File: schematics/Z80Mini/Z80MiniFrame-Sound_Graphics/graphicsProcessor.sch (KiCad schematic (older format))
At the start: 18 parts, among them J2 RGB Out, U1 TMS9929A, U12 74LS32, U2 74LS574, U3 74LS574, U4 74LS574, U5 AS6C62256-55PCN, U6 74HC04, Y1 Crystal

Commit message: Latest graphics and sound card schematic and PCB modifications
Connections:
- wire segments 226 -> 227
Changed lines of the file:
@@
 L power:VCC #PWR0103
 U 1 1 5D7AF4D2
-P 9100 750
-F 0 "#PWR0103" H 9100 600 50  0001 C CNN
-F 1 "VCC" H 9117 923 50  0000 C CNN
-F 2 "" H 9100 750 50  0001 C CNN
-F 3 "" H 9100 750 50  0001 C CNN
-	1    9100 750
+P 7850 750
+F 0 "#PWR0103" H 7850 600 50  0001 C CNN
+F 1 "VCC" H 7867 923 50  0000 C CNN
+F 2 "" H 7850 750 50  0001 C CNN
+F 3 "" H 7850 750 50  0001 C CNN
+	1    7850 750
 	1    0    0    -1
 $EndComp
@@
 	6600 950  6600 850
 Wire Wire Line
-	6600 850  9100 850
+	6600 850  7850 850
 Connection ~ 9100 850
 Wire Wire Line
-	9100 850  9100 750
+	7850 850  7850 750
 Wire Wire Line
 	7100 1350 7250 1350
@@
 Wire Wire Line
 	1250 2500 1650 2500
-Wire Wire Line
-	3950 2350 4250 2350
-Wire Wire Line
-	9000 1450 9800 1450
-Wire Wire Line
-	9000 1950 9700 1950
-Wire Bus Line
-	7700 2450 7700 3000
-Wire Bus Line
-	9250 2350 9250 3000
-Wire Bus Line
-	9250 1050 9250 1950
-Wire Bus Line
-	2800 1050 2800 2950
-Wire Bus Line
-	4150 3350 4150 6850
-Wire Bus Line
-	4150 1050 4150 3050
-Wire Bus Line
-	7800 1050 7800 2150
-Wire Bus Line
-	7350 1050 7350 3700
-Wire Bus Line
-	7700 3000 7700 6850
-Wire Bus Line
-	5850 1050 5850 5550
 $Comp
 L power:GND #PWR0145
@@
 $EndComp
 Connection ~ 1650 1500
+Connection ~ 7850 850
+Wire Wire Line
+	7850 850  9100 850
+Wire Wire Line
+	3950 2350 4250 2350
+Wire Wire Line
+	9000 1450 9800 1450
+Wire Wire Line
+	9000 1950 9700 1950
+Wire Bus Line
+	7700 2450 7700 3000
+Wire Bus Line
+	9250 2350 9250 3000
+Wire Bus Line
+	9250 1050 9250 1950
+Wire Bus Line
+	2800 1050 2800 2950
+Wire Bus Line
+	4150 3350 4150 6850
+Wire Bus Line
+	4150 1050 4150 3050
+Wire Bus Line
+	7800 1050 7800 2150
+Wire Bus Line
+	7350 1050 7350 3700
+Wire Bus Line
+	7700 3000 7700 6850
+Wire Bus Line
+	5850 1050 5850 5550
 $EndSCHEMATC

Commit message: Latest modifications
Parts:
- C16, C17: value 100nF -> 22pF
- U1: symbol Video:TMS9929A -> Z80MiniFrame-Sound_Graphics-rescue:TMS9929A-Video
- U5: symbol Memory_RAM:AS6C62256-55PCN -> Z80MiniFrame-Sound_Graphics-rescue:AS6C62256-55PCN-Memory_RAM
- Y1: value Crystal -> 10MHz
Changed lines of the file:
@@
 $EndDescr
 $Comp
-L Video:TMS9929A U1
+L Z80MiniFrame-Sound_Graphics-rescue:TMS9929A-Video U1
 U 1 1 5D79CD27
 P 3400 1950
@@
 	7350 1050 7800 1050
 $Comp
-L Memory_RAM:AS6C62256-55PCN U5
+L Z80MiniFrame-Sound_Graphics-rescue:AS6C62256-55PCN-Memory_RAM U5
 U 1 1 5D7A4B8E
 P 8000 1350
@@
 P 2000 3150
 F 0 "Y1" V 1954 3281 50  0000 L CNN
-F 1 "Crystal" V 2045 3281 50  0000 L CNN
+F 1 "10MHz" V 2045 3281 50  0000 L CNN
 F 2 "Crystal:Crystal_HC18-U_Vertical" H 2000 3150 50  0001 C CNN
 F 3 "~" H 2000 3150 50  0001 C CNN
@@
 AR Path="/5D79B46A/5DF21B0E" Ref="C16"  Part="1"
 F 0 "C16" V 1348 3000 50  0000 C CNN
-F 1 "100nF" V 1439 3000 50  0000 C CNN
+F 1 "22pF" V 1439 3000 50  0000 C CNN
 F 2 "Capacitor_THT:C_Disc_D7.0mm_W2.5mm_P5.00mm" H 1638 2850 50  0001 C CNN
 F 3 "~" H 1600 3000 50  0001 C CNN
@@
 AR Path="/5D79B46A/5DF22922" Ref="C17"  Part="1"
 F 0 "C17" V 1348 3300 50  0000 C CNN
-F 1 "100nF" V 1439 3300 50  0000 C CNN
+F 1 "22pF" V 1439 3300 50  0000 C CNN
 F 2 "Capacitor_THT:C_Disc_D7.0mm_W2.5mm_P5.00mm" H 1638 3150 50  0001 C CNN
 F 3 "~" H 1600 3300 50  0001 C CNN

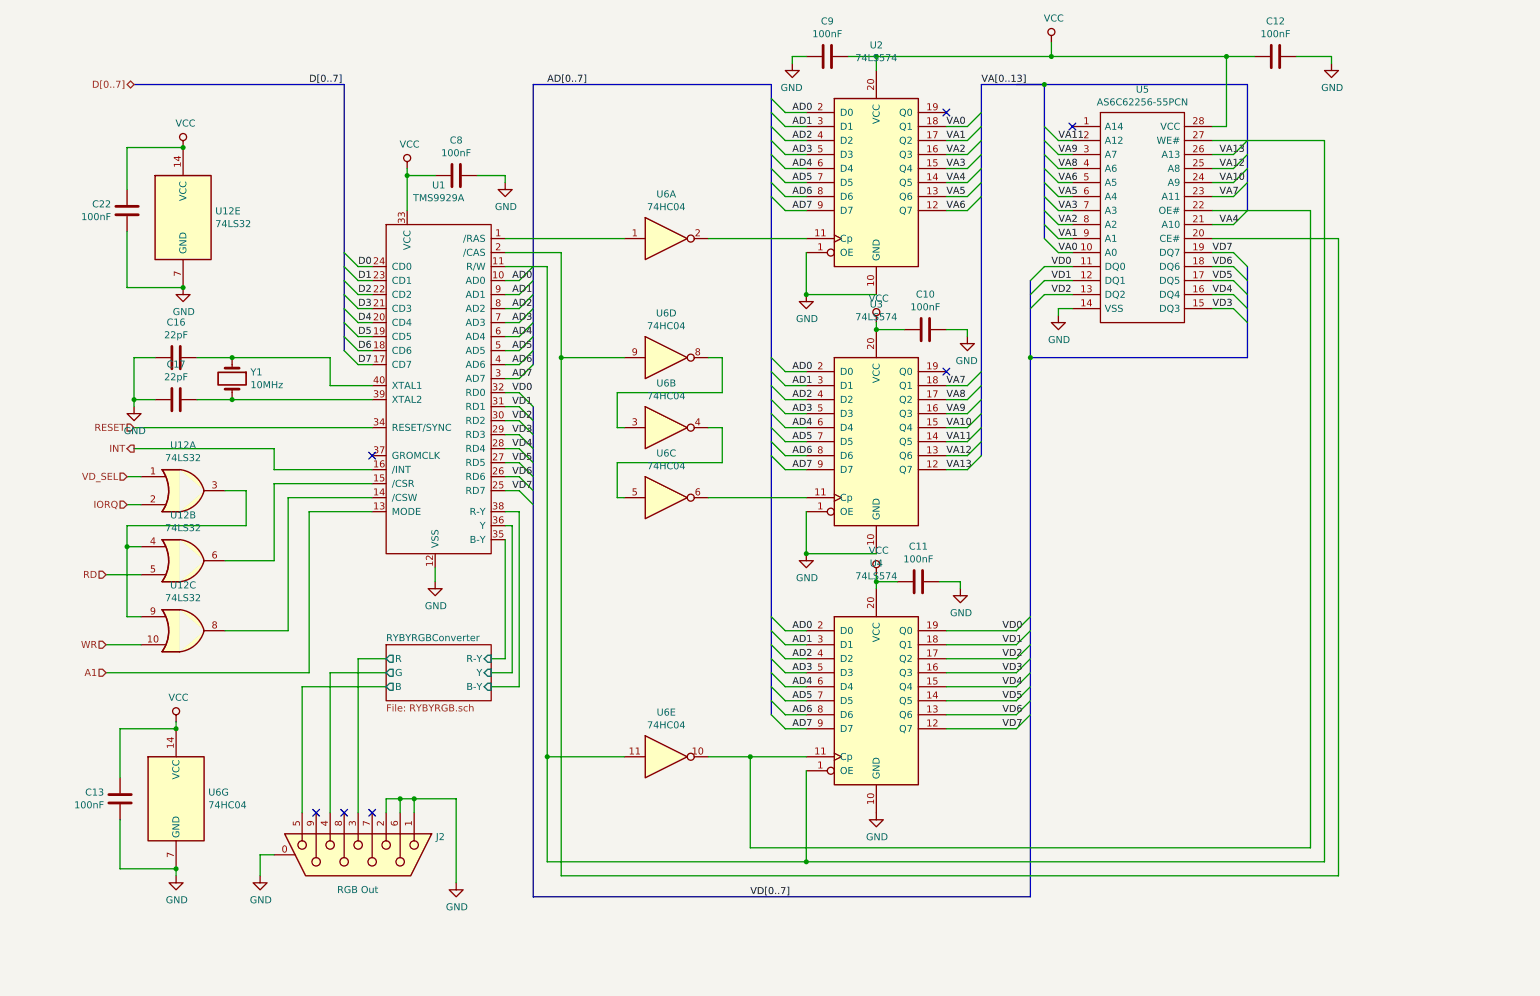
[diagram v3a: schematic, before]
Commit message: Latest modifications and update to v1.1 and first successifully VDP routines test.
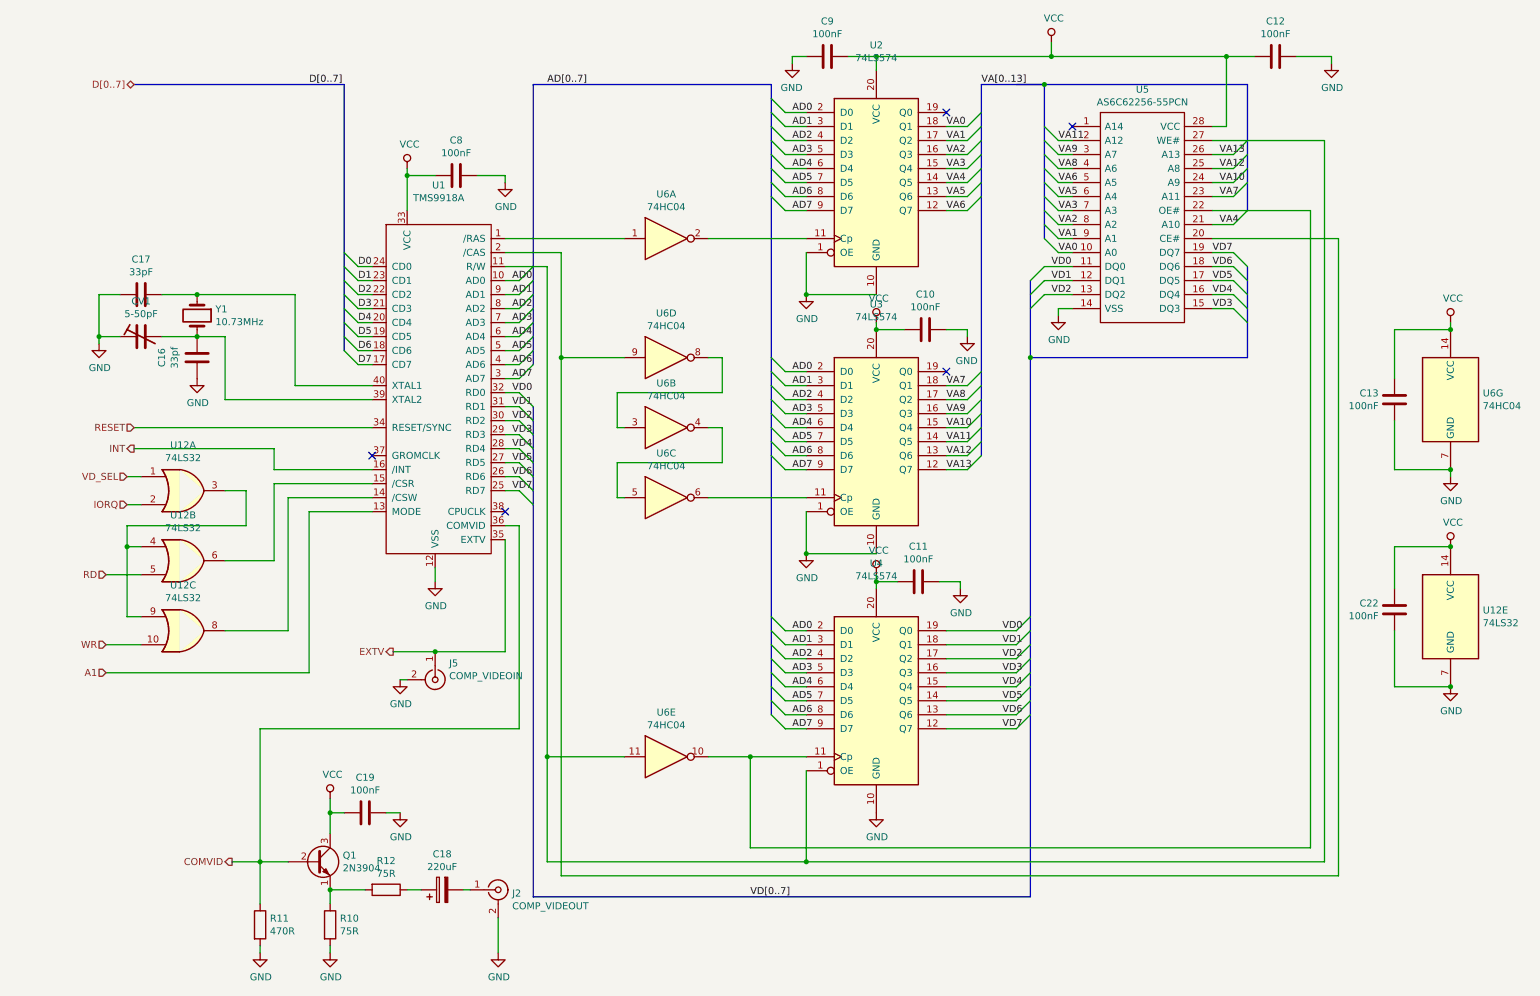
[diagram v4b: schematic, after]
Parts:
- removed J2: RGB Out, Connector_Dsub:DSUB-9_Female_Horizontal_P2.77x2.84mm_EdgePinOffset4.94mm_Housed_MountingHolesOffset7.48mm, symbol Connector:DB9_Female_MountingHoles
- removed U1: TMS9929A, Package_DIP:DIP-40_W15.24mm_LongPads, symbol Z80MiniFrame-Sound_Graphics-rescue:TMS9929A-Video
- added C18: 220uF, Capacitor_THT:CP_Radial_Tantal_D6.0mm_P2.50mm, symbol Device:CP
- added C19: 100nF, Capacitor_THT:C_Disc_D7.0mm_W2.5mm_P5.00mm, symbol Device:C
- added CV1: 5-50pF, Potentiometer_THT:Potentiometer_ACP_CA9-V10_Vertical, symbol Device:CTRIM
- added J2: COMP_VIDEOUT, Connector:RCA_Female_902, symbol Connector:Conn_Coaxial
- added J5: COMP_VIDEOIN, Connector:RCA_Female_902, symbol Connector:Conn_Coaxial
- added Q1: 2N3904, Package_TO_SOT_THT:TO-92_Inline, symbol Transistor_BJT:2N3904
- added R10, R12: 75R, Resistor_THT:R_Axial_DIN0207_L6.3mm_D2.5mm_P10.16mm_Horizontal, symbol Device:R
- added R11: 470R, Resistor_THT:R_Axial_DIN0207_L6.3mm_D2.5mm_P10.16mm_Horizontal, symbol Device:R
- added U1: TMS9918A, Package_DIP:DIP-40_W15.24mm_LongPads, symbol Video:TMS9918A
- C16: value 22pF -> 33pf
- C17: value 22pF -> 33pF
- Y1: value 10MHz -> 10.73MHz
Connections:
- net A1: now also U1.13 (MODE)
- net AD0: now also U1.10 (AD0)
- net AD1: now also U1.9 (AD1)
- net AD2: now also U1.8 (AD2)
- net AD3: now also U1.7 (AD3)
- net AD4: now also U1.6 (AD4)
- net AD5: now also U1.5 (AD5)
- net AD6: now also U1.4 (AD6)
- net AD7: now also U1.3 (AD7)
- net D0: now also U1.24 (CD0)
- net D1: now also U1.23 (CD1)
- net D2: now also U1.22 (CD2)
- net D3: now also U1.21 (CD3)
- net D4: now also U1.20 (CD4)
- net D5: now also U1.19 (CD5)
- net D6: now also U1.18 (CD6)
- net D7: now also U1.17 (CD7)
- net GND: now also C19.1, CV1.1, J2.2 (Ext), J5.2 (Ext), R10.2, R11.2, U1.12 (VSS)
- net INT: now also U1.16 (/INT)
- net RESET: now also U1.34 (RESET/SYNC)
- net VCC: now also C19.2, Q1.3 (C), U1.33 (VCC)
- net VD0: now also U1.32 (RD0)
- net VD1: now also U1.31 (RD1)
- net VD2: now also U1.30 (RD2)
- net VD3: now also U1.29 (RD3)
- net VD4: now also U1.28 (RD4)
- net VD5: now also U1.27 (RD5)
- net VD6: now also U1.26 (RD6)
- net VD7: now also U1.25 (RD7)
- net at U6.1: now also U1.1 (/RAS)
- net at U4.1 (OE), U5.27 (WE#), U6.11: now also U1.11 (R/W)
- net at U12.8: now also U1.14 (/CSW)
- net at U12.6: now also U1.15 (/CSR)
- net at U5.20 (CE#), U6.9: now also U1.2 (/CAS)
- net at C17.2: now also Y1.1, U1.40 (XTAL1); no longer Y1.2
- net at C16.2: now also Y1.2, CV1.2, U1.39 (XTAL2); no longer Y1.1
- new net: Q1.1 (E), R10.1, R12.2
- new net: C18.1, R12.1
- new net: C18.2, J2.1 (In)
- new net COMVID: Q1.2 (B), R11.1, U1.36 (COMVID)
- new net EXTV: J5.1 (In), U1.35 (EXTV)
- no-connect marks 7 -> 5
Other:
- moved on the sheet: C13, C16, C17, C22, U12E, U6G, Y1

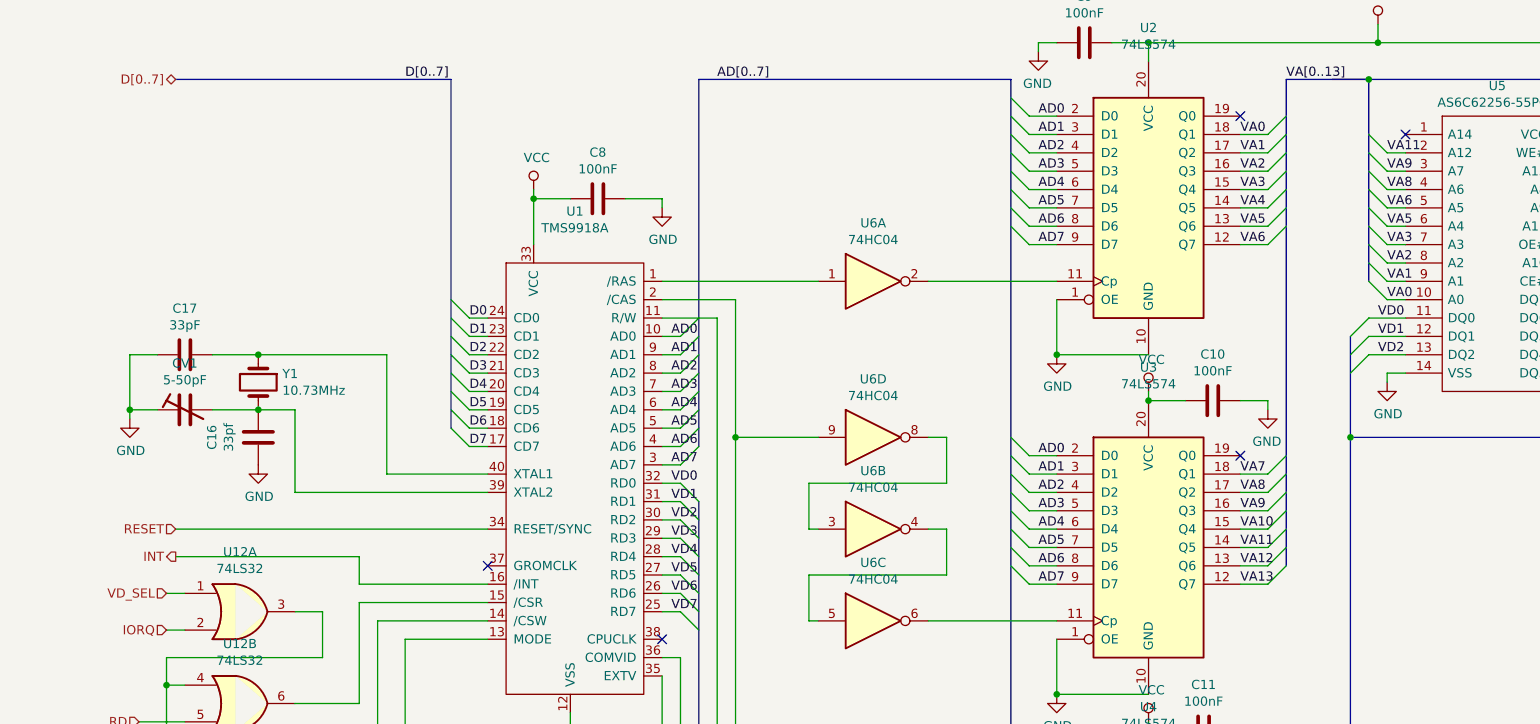
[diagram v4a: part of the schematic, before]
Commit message: Added new code for core written in C with Z88DK
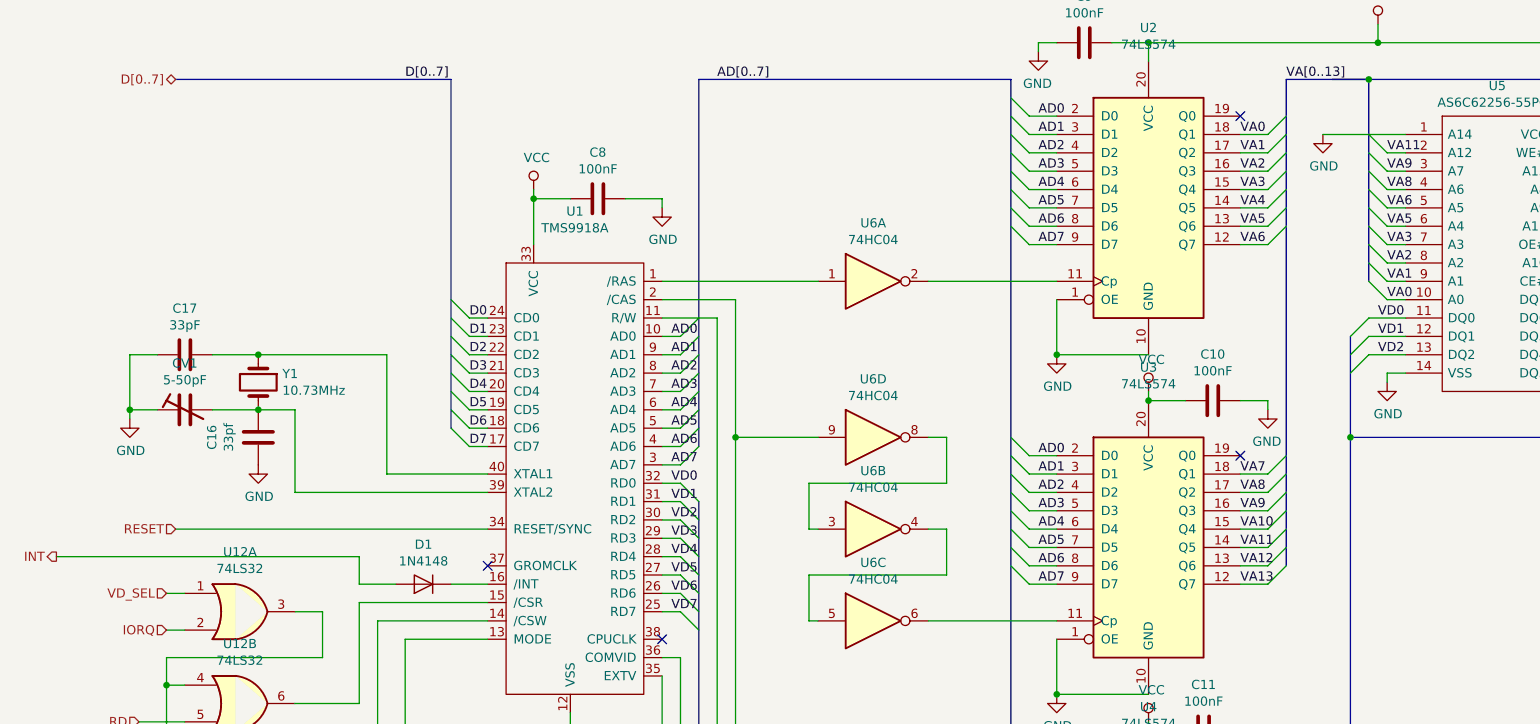
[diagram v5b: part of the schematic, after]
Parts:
- added D1: 1N4148, Diode_THT:D_DO-35_SOD27_P7.62mm_Horizontal, symbol Diode:1N4148
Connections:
- net GND: now also U5.1 (A14)
- net INT: now also D1.2 (A); no longer U1.16 (/INT)
- new net: D1.1 (K), U1.16 (/INT)
- no-connect marks 5 -> 4
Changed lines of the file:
@@
 	1    0    0    -1
 $EndComp
-NoConn ~ 8000 1350
 Wire Wire Line
 	6600 950  6600 850
@@
 	1    0    0    -1
 $EndComp
-Text HLabel 1300 3650 0    50   Output ~ 0
+Text HLabel 650  3650 0    50   Output ~ 0
 INT
 Wire Wire Line
-	2300 3650 1300 3650
-Wire Wire Line
 	2300 3800 2300 3650
-Wire Wire Line
-	3000 3800 2300 3800
 $Comp
 L power:GND #PWR0132
@@
 Wire Wire Line
 	2000 6600 2200 6600
+$Comp
+L power:GND #PWR0138
+U 1 1 5DF966DD
+P 7550 1350
+F 0 "#PWR0138" H 7550 1100 50  0001 C CNN
+F 1 "GND" H 7555 1177 50  0000 C CNN
+F 2 "" H 7550 1350 50  0001 C CNN
+F 3 "" H 7550 1350 50  0001 C CNN
+	1    7550 1350
+	1    0    0    -1
+$EndComp
+Wire Wire Line
+	650  3650 2300 3650
+$Comp
+L Diode:1N4148 D1
+U 1 1 5E052EE5
+P 2650 3800
+F 0 "D1" H 2650 3584 50  0000 C CNN
+F 1 "1N4148" H 2650 3675 50  0000 C CNN
+F 2 "Diode_THT:D_DO-35_SOD27_P7.62mm_Horizontal" H 2650 3625 50  0001 C CNN
+F 3 "https://assets.nexperia.com/documents/data-sheet/1N4148_1N4448.pdf" H 2650 3800 50  0001 C CNN
+	1    2650 3800
+	-1   0    0    1
+$EndComp
+Wire Wire Line
+	2500 3800 2300 3800
+Wire Wire Line
+	2800 3800 3000 3800
 Wire Wire Line
 	9000 1450 9800 1450
@@
 Wire Wire Line
 	3950 2350 4250 2350
+Wire Wire Line
+	7550 1350 8000 1350
 Wire Bus Line
 	7700 2450 7700 3000
